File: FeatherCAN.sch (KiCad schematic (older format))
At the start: 28 parts, among them J1 feather long, J2 feather short, J3 Header, J4 PicoBlade, U1 DS3231MZ, U2 MCP2515-xST, U3 MCP2551-I-SN, U4 5V, Y1 16MHz

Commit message: first version sent for production review
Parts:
- BT1: MFN (none) -> Linx Technologies; MFP (none) -> BAT-HLD-012-SMT-TR; SKU (none) -> BAT-HLD-012-SMTCT-ND; Vendor (none) -> Digikey
- C1, C2: Characteristics (none) -> X5R 20V
- C3, C4: Characteristics (none) -> NPO 6V
- C5, C6: Characteristics (none) -> X7R 6V
- D1: SKU (none) -> 754-1931-1-ND; Vendor (none) -> Digikey
- D3: value Green -> PWR
- J1: value feather long -> Feather Long; Config (none) -> nofit
- J2: value feather short -> Feather Short; Config (none) -> nofit
- J4: SKU (none) -> WM7622CT-ND; Vendor (none) -> Digikey
- JP1: Notes (none) -> Link to bring termination resistor in circuit
- JP2: Notes (none) -> Cut to remove INT connection to Feather
- U1: MFN (none) -> Maxim; MFP (none) -> DS3231MZ+; SKU (none) -> DS3231MZ+-ND; Vendor (none) -> Digikey
- U3: MFP MCP1703A-3302_SOT23 -> MCP2551-I/SN; SKU (none) -> MCP2551-I/SN-ND; Vendor (none) -> Digikey
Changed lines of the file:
@@
 P 8600 2000
 F 0 "J1" H 8519 975 50  0000 C CNN
-F 1 "feather long" H 8519 1066 50  0000 C CNN
+F 1 "Feather Long" H 8519 1066 50  0000 C CNN
 F 2 "KiCad/Connector_PinHeader_2.54mm.pretty:PinHeader_1x16_P2.54mm_Vertical" H 8600 2000 50  0001 C CNN
 F 3 "~" H 8600 2000 50  0001 C CNN
+F 4 "nofit" H 8600 2000 50  0001 C CNN "Config"
 	1    8600 2000
 	1    0    0    1
@@
 F 3 "http://ww1.microchip.com/downloads/en/devicedoc/21667d.pdf" H 2800 4950 50  0001 C CNN
 F 4 "Microship" H 2800 4950 50  0001 C CNN "MFN"
-F 5 "MCP1703A-3302_SOT23" H 2800 4950 50  0001 C CNN "MFP"
+F 5 "MCP2551-I/SN" H 2800 4950 50  0001 C CNN "MFP"
 F 6 "3.3 V 250 mA upto 16 V input" H 2800 4950 50  0001 C CNN "Description"
+F 7 "Digikey" H 2800 4950 50  0001 C CNN "Vendor"
+F 8 "MCP2551-I/SN-ND" H 2800 4950 50  0001 C CNN "SKU"
 	1    2800 4950
 	-1   0    0    -1
@@
 F 2 "KiCad/Package_SO.pretty:SOIC-8_3.9x4.9mm_P1.27mm" H 9050 4300 50  0001 C CNN
 F 3 "http://datasheets.maximintegrated.com/en/ds/DS3231M.pdf" H 9050 4200 50  0001 C CNN
+F 4 "Maxim" H 9050 4800 50  0001 C CNN "MFN"
+F 5 "DS3231MZ+" H 9050 4800 50  0001 C CNN "MFP"
+F 6 "Digikey" H 9050 4800 50  0001 C CNN "Vendor"
+F 7 "DS3231MZ+-ND " H 9050 4800 50  0001 C CNN "SKU"
 	1    9050 4800
 	1    0    0    -1
@@
 F 2 "KiCad/Battery.pretty:BatteryHolder_LINX_BAT-HLD-012-SMT" V 8550 4160 50  0001 C CNN
 F 3 "~" V 8550 4160 50  0001 C CNN
+F 4 "Linx Technologies" H 8550 4100 50  0001 C CNN "MFN"
+F 5 "BAT-HLD-012-SMT-TR" H 8550 4100 50  0001 C CNN "MFP"
+F 6 "Digikey" H 8550 4100 50  0001 C CNN "Vendor"
+F 7 "BAT-HLD-012-SMTCT-ND" H 8550 4100 50  0001 C CNN "SKU"
 	1    8550 4100
 	0    1    1    0
@@
 F 2 "KiCad/Capacitor_SMD.pretty:C_0603_1608Metric" H 4338 1850 50  0001 C CNN
 F 3 "~" H 4300 2000 50  0001 C CNN
+F 4 "X5R 20V" H 4300 2000 50  0001 C CNN "Characteristics"
 	1    4300 2000
 	1    0    0    -1
@@
 F 6 "Orange 605nm LED Indication - Discrete 1.8V 2mA 0603 (1608 Metric)" H 3850 3950 60  0001 C CNN "Description"
 F 7 "Orange" H 3850 3950 50  0001 C CNN "Characteristics"
+F 8 "754-1931-1-ND " H 3850 3950 50  0001 C CNN "SKU"
+F 9 "Digikey" H 3850 3950 50  0001 C CNN "Vendor"
 	1    3850 3950
 	0    -1   -1   0
@@
 F 3 "~" H 4600 5450 50  0001 C CNN
 F 4 "nofit" H 4600 5450 50  0001 C CNN "Config"
+F 5 "Cut to remove INT connection to Feather" H 4600 5450 50  0001 C CNN "Notes"
 	1    4600 5450
 	1    0    0    -1
@@
 F 2 "KiCad/Capacitor_SMD.pretty:C_0603_1608Metric" H 8638 3650 50  0001 C CNN
 F 3 "~" H 8600 3800 50  0001 C CNN
+F 4 "X7R 6V" H 8600 3800 50  0001 C CNN "Characteristics"
 	1    8600 3800
 	0    1    1    0
@@
 F 3 "~" H 2100 5250 50  0001 C CNN
 F 4 "nofit" H 2100 5250 50  0001 C CNN "Config"
+F 5 "Link to bring termination resistor in circuit" H 2100 5250 50  0001 C CNN "Notes"
 	1    2100 5250
 	0    1    1    0
@@
 F 2 "KiCad/Capacitor_SMD.pretty:C_0603_1608Metric" H 2888 1850 50  0001 C CNN
 F 3 "~" H 2850 2000 50  0001 C CNN
+F 4 "X5R 20V" H 2850 2000 50  0001 C CNN "Characteristics"
 	1    2850 2000
 	1    0    0    -1
@@
 P 5700 1400
 F 0 "D3" H 5700 1500 50  0000 C CNN
-F 1 "Green" H 5700 1300 50  0000 C CNN
+F 1 "PWR" H 5700 1300 50  0000 C CNN
 F 2 "KiCad/LED_SMD.pretty:LED_0603_1608Metric" H 5700 1400 50  0001 C CNN
 F 3 "http://www.kingbrightusa.com/images/catalog/SPEC/APT1608LZGCK.pdf" H 5700 1400 50  0001 C CNN
@@
 P 9000 2200
 F 0 "J2" H 8920 1375 50  0000 C CNN
-F 1 "feather short" H 8920 1466 50  0000 C CNN
+F 1 "Feather Short" H 8920 1466 50  0000 C CNN
 F 2 "KiCad/Connector_PinHeader_2.54mm.pretty:PinHeader_1x12_P2.54mm_Vertical" H 9000 2200 50  0001 C CNN
 F 3 "~" H 9000 2200 50  0001 C CNN
+F 4 "nofit" H 9000 2200 50  0001 C CNN "Config"
 	1    9000 2200
 	-1   0    0    1
@@
 F 2 "KiCad/Capacitor_SMD.pretty:C_0603_1608Metric" H 6988 5400 50  0001 C CNN
 F 3 "~" H 6950 5550 50  0001 C CNN
+F 4 "NPO 6V" H 6950 5550 50  0001 C CNN "Characteristics"
 	1    6950 5550
 	-1   0    0    1
@@
 F 2 "KiCad/Capacitor_SMD.pretty:C_0603_1608Metric" H 6588 5800 50  0001 C CNN
 F 3 "~" H 6550 5950 50  0001 C CNN
+F 4 "NPO 6V" H 6550 5950 50  0001 C CNN "Characteristics"
 	1    6550 5950
 	-1   0    0    1
@@
 F 2 "KiCad/Capacitor_SMD.pretty:C_0603_1608Metric" H 5788 3800 50  0001 C CNN
 F 3 "~" H 5750 3950 50  0001 C CNN
+F 4 "X7R 6V" H 5750 3950 50  0001 C CNN "Characteristics"
 	1    5750 3950
 	0    1    1    0
@@
 F 4 "Molex" H 1400 2900 50  0001 C CNN "MFN"
 F 5 "53261-0471" H 1400 2900 50  0001 C CNN "MFP"
+F 6 "Digikey" H 1400 2900 50  0001 C CNN "Vendor"
+F 7 "WM7622CT-ND" H 1400 2900 50  0001 C CNN "SKU"
 	1    1400 2900
 	1    0    0    -1

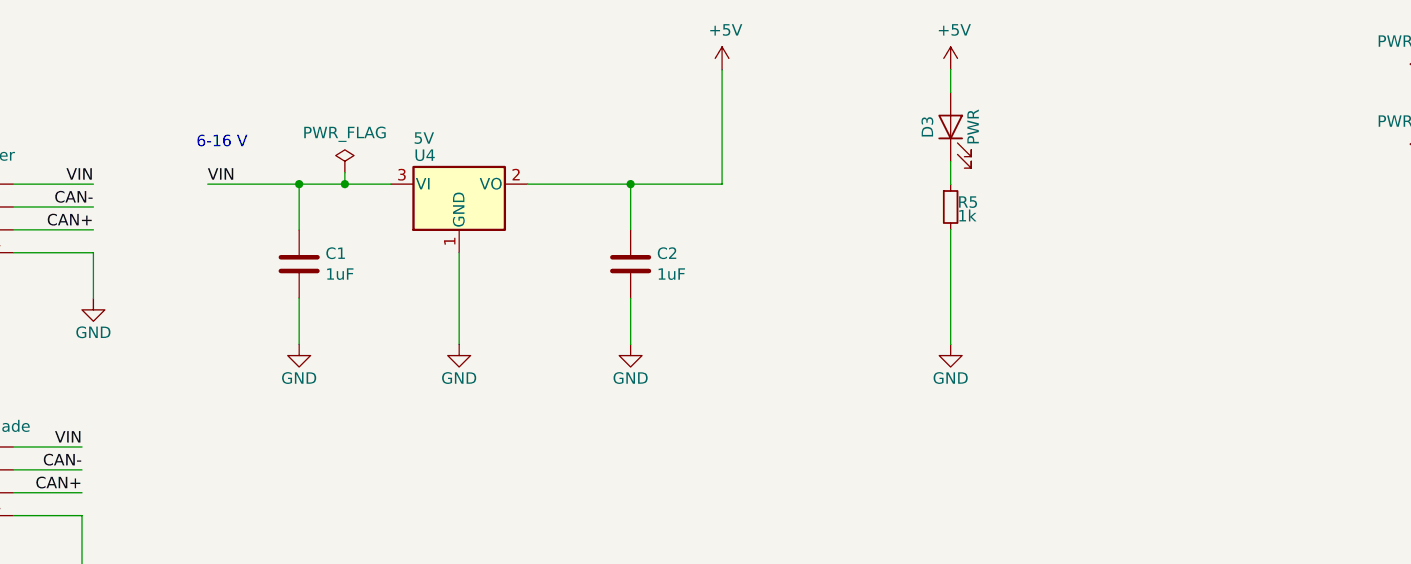
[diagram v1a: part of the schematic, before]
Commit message: reverse polority protect and clamp VIN
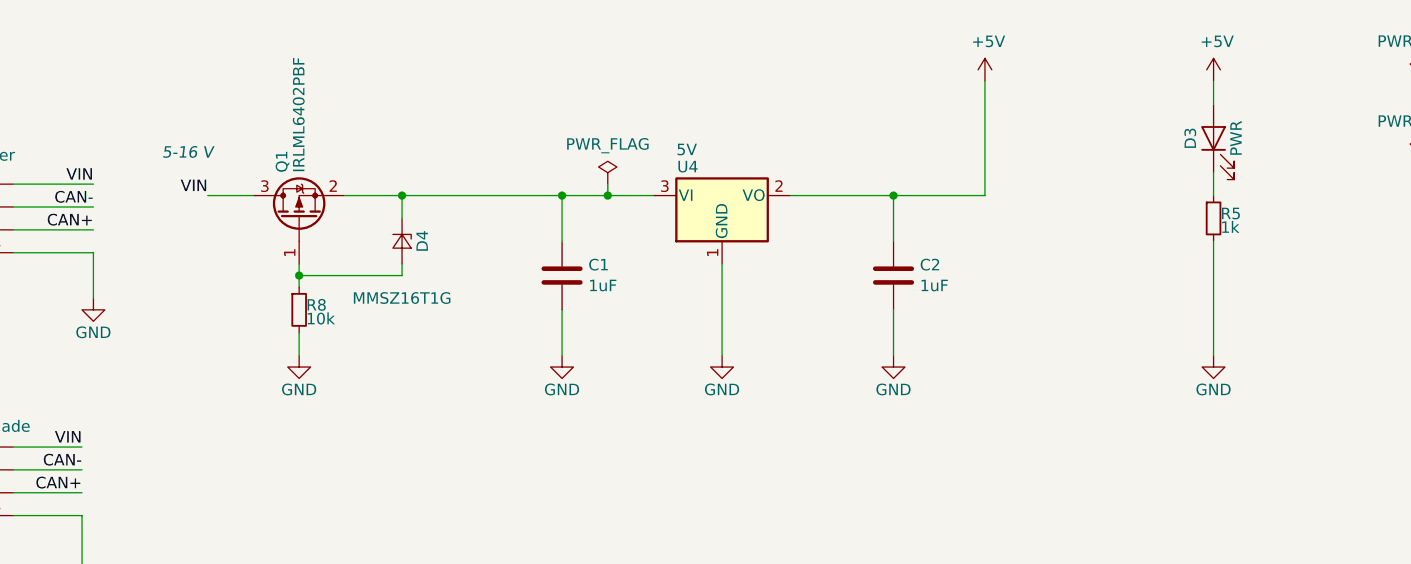
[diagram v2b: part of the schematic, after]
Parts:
- added D4: MMSZ16T1G, KiCad/Diode_SMD.pretty:D_SOD-123, symbol Device:D_Zener_Small
- added Q1: IRLML6402PBF, KiCad/Package_TO_SOT_SMD.pretty:SOT-23, symbol Transistor_FET:TP0610T
- added R8: 10k, KiCad/Resistor_SMD.pretty:R_0603_1608Metric, symbol Device:R_Small
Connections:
- net GND: now also R8.2
- net VIN: now also Q1.3 (D); no longer C1.1, U4.3 (VI)
- new net: C1.1, D4.1 (K), Q1.2 (S), U4.3 (VI)
- new net: D4.2 (A), Q1.1 (G), R8.1
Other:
- note added: "5-16 V"
- note removed: "6-16 V"
- moved on the sheet: C1, C2, U4

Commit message: add part numbers
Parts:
- U2: MFN (none) -> Microchip Technology; MFP (none) -> MCP2515T-I/ST; SKU (none) -> MCP2515T-I/STCT-ND; Vendor (none) -> Digikey
- U3: MFN Microship -> Microchip Technology
- U4: symbol Regulator_Linear:MCP1703A-3302_SOT23 -> Regulator_Linear:MCP1700-5002E_SOT23; MFN Microchip -> Microchip Technology
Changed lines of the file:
@@
 F 2 "KiCad/Package_SO.pretty:SOIC-8_3.9x4.9mm_P1.27mm" H 2800 4450 50  0001 C CIN
 F 3 "http://ww1.microchip.com/downloads/en/devicedoc/21667d.pdf" H 2800 4950 50  0001 C CNN
-F 4 "Microship" H 2800 4950 50  0001 C CNN "MFN"
+F 4 "Microchip Technology" H 2800 4950 50  0001 C CNN "MFN"
 F 5 "MCP2551-I/SN" H 2800 4950 50  0001 C CNN "MFP"
 F 6 "3.3 V 250 mA upto 16 V input" H 2800 4950 50  0001 C CNN "Description"
@@
 Connection ~ 5450 1700
 $Comp
-L Regulator_Linear:MCP1703A-3302_SOT23 U4
+L Regulator_Linear:MCP1700-5002E_SOT23 U4
 U 1 1 5AB155FD
 P 4700 1700
@@
 F 2 "KiCad/Package_TO_SOT_SMD.pretty:SOT-23" H 4700 1900 50  0001 C CNN
 F 3 "http://www.microchip.com/mymicrochip/filehandler.aspx?ddocname=en530937" H 4700 1650 50  0001 C CNN
-F 4 "Microchip" H 4700 1700 60  0001 C CNN "MFN"
+F 4 "Microchip Technology" H 4700 1700 60  0001 C CNN "MFN"
 F 5 "MCP1703T-5002E/CB" H 4700 1700 60  0001 C CNN "MFP"
 F 6 "5 V LDO" H 4700 1700 60  0001 C CNN "Description"
@@
 F 2 "KiCad/Package_SO.pretty:TSSOP-20_4.4x6.5mm_P0.65mm" H 5400 4550 50  0001 C CIN
 F 3 "http://ww1.microchip.com/downloads/en/DeviceDoc/21801e.pdf" H 5500 4650 50  0001 C CNN
+F 4 "Microchip Technology" H 5400 5450 50  0001 C CNN "MFN"
+F 5 "MCP2515T-I/ST" H 5400 5450 50  0001 C CNN "MFP"
+F 6 "MCP2515T-I/STCT-ND" H 5400 5450 50  0001 C CNN "SKU"
+F 7 "Digikey" H 5400 5450 50  0001 C CNN "Vendor"
 	1    5400 5450
 	-1   0    0    -1

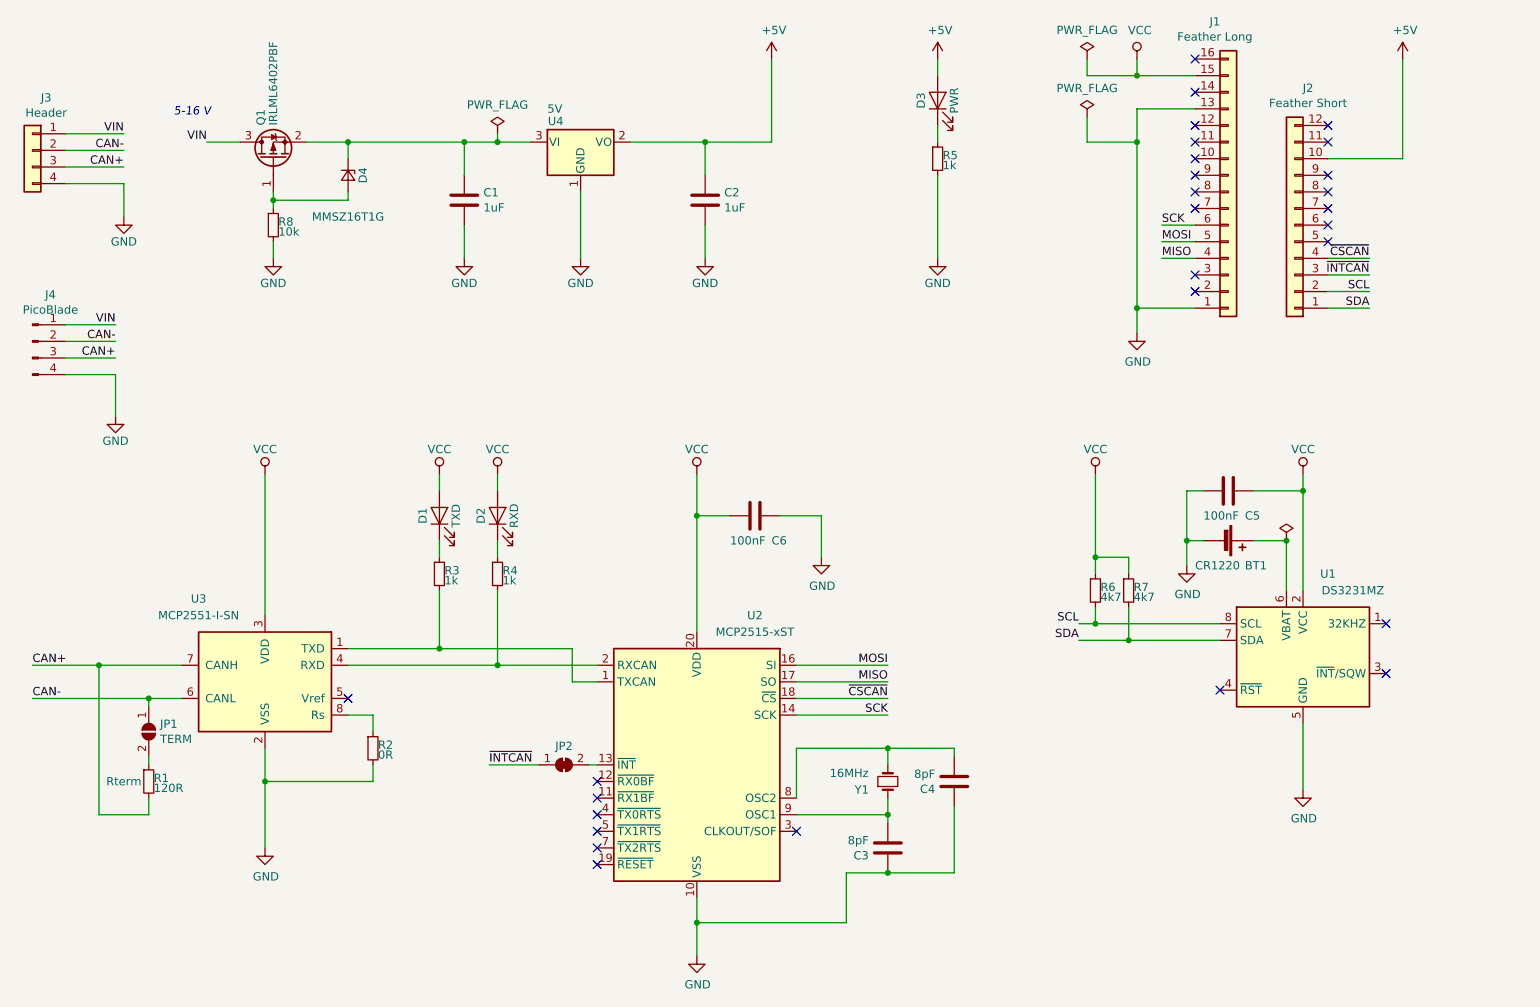
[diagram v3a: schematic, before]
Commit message: pull-up on MCP reset and fix 4-pad crystal pins
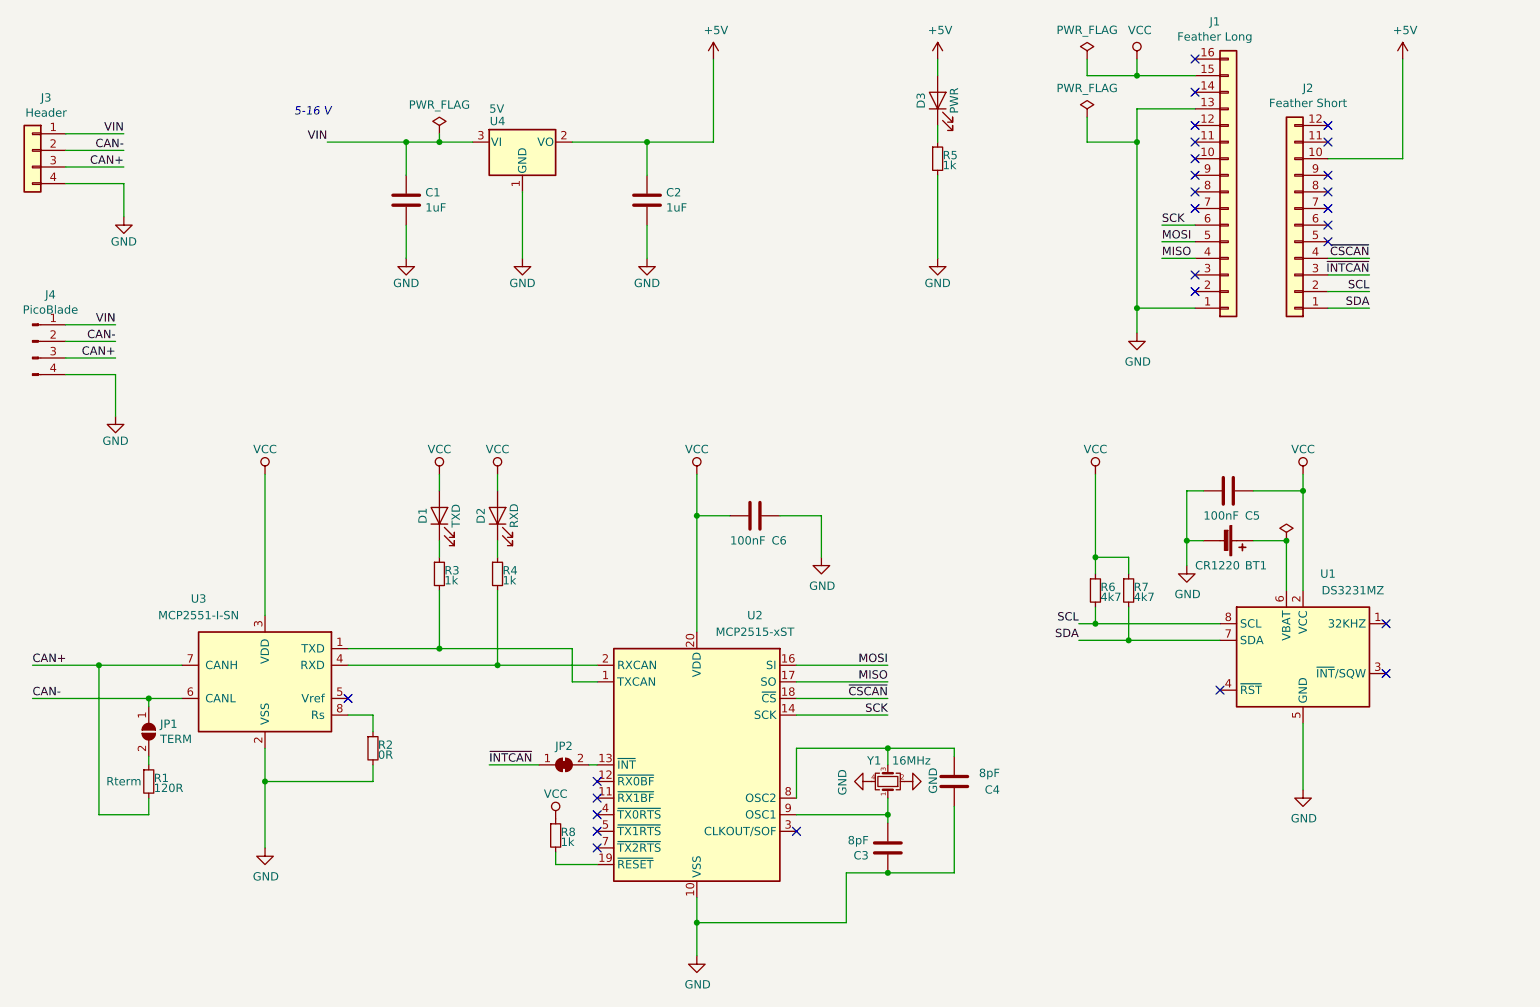
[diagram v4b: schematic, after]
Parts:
- removed D4: MMSZ16T1G, KiCad/Diode_SMD.pretty:D_SOD-123, symbol Device:D_Zener_Small
- removed Q1: IRLML6402PBF, KiCad/Package_TO_SOT_SMD.pretty:SOT-23, symbol Transistor_FET:TP0610T
- removed Y1: 16MHz, KiCad/Crystal.pretty:Crystal_SMD_3225-4Pin_3.2x2.5mm, symbol Device:Crystal_Small
- added Y1: 16MHz, KiCad/Crystal.pretty:Crystal_SMD_3225-4Pin_3.2x2.5mm, symbol Device:Crystal_GND24_Small
- R8: value 10k -> 1k
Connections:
- net GND: now also Y1.2, Y1.4; no longer R8.2
- net VCC: now also R8.1
- net VIN: now also C1.1, U4.3 (VI)
- net at U2.19 (~RESET): now also R8.2
- net at C4.2, U2.8 (OSC2): now also Y1.3
- net at C3.2, U2.9 (OSC1): now also Y1.1
- no-connect marks 28 -> 27
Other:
- moved on the sheet: C1, C2, U4
